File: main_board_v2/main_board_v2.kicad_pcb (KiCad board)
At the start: 2 copper layers, 13 parts, among them J1 Raspberry_Pi_4, U1 Pico, U2 Pico

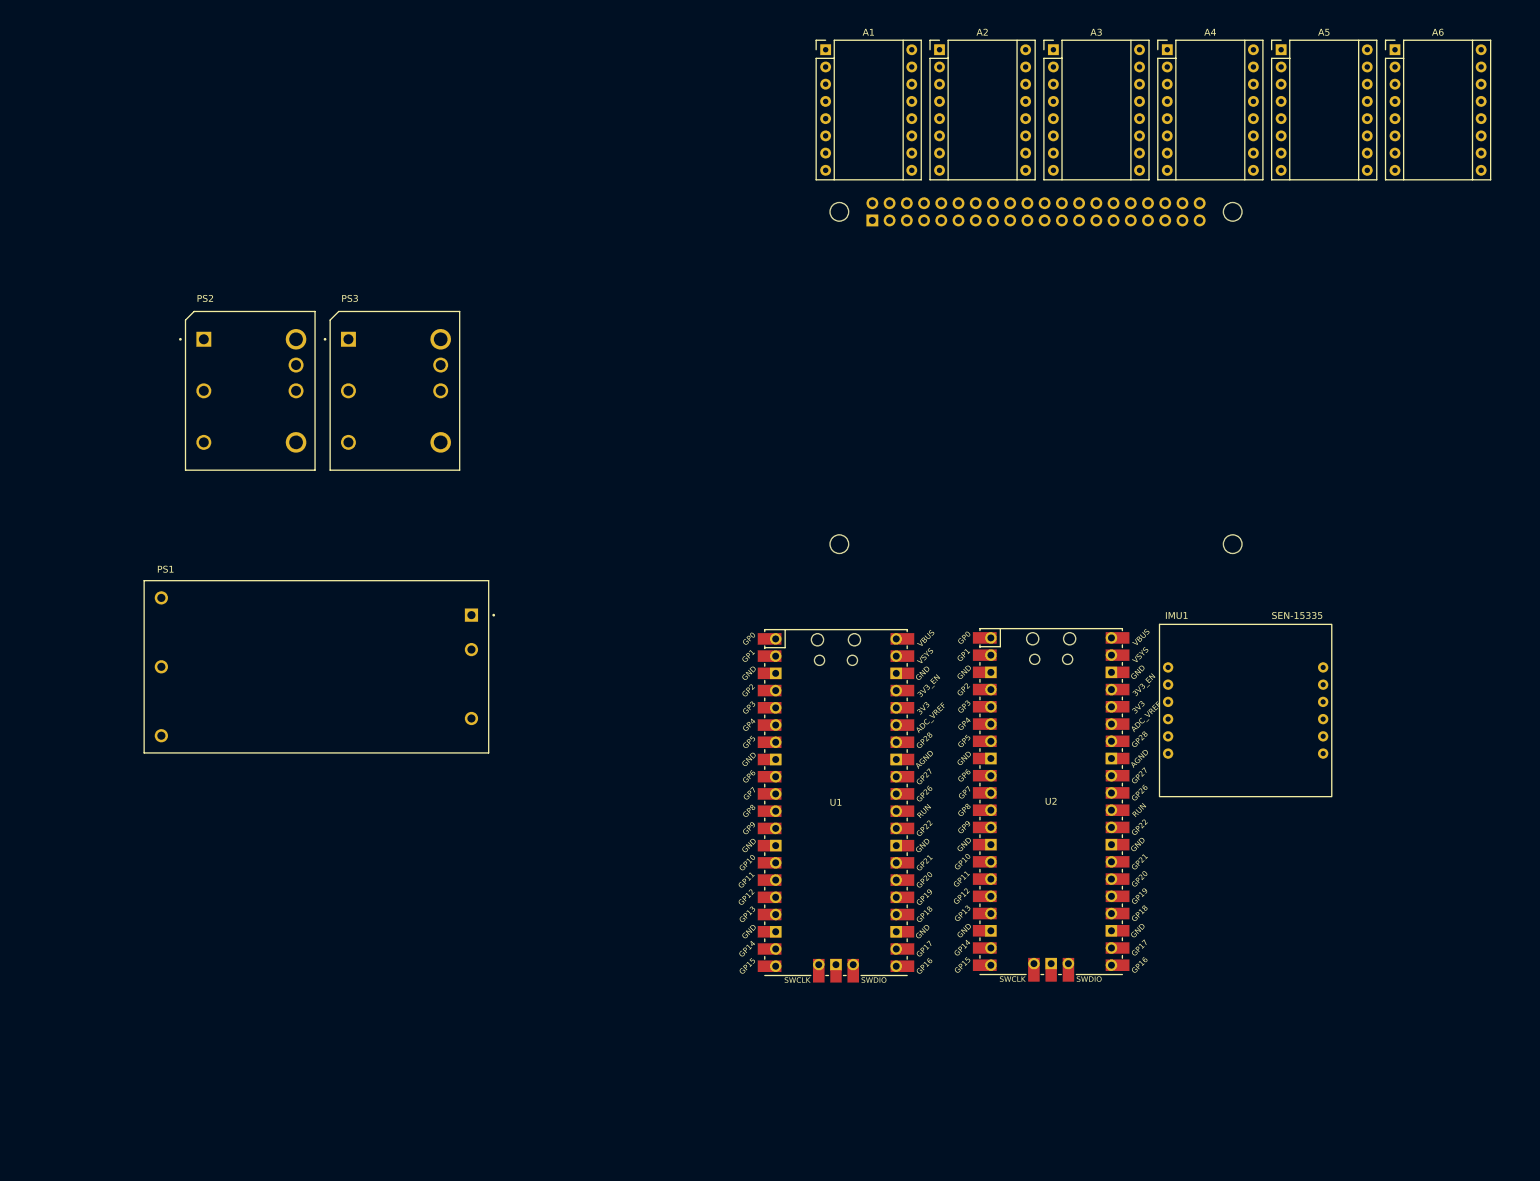
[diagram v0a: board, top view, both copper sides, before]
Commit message: Added headers and corrected 3d model of pico
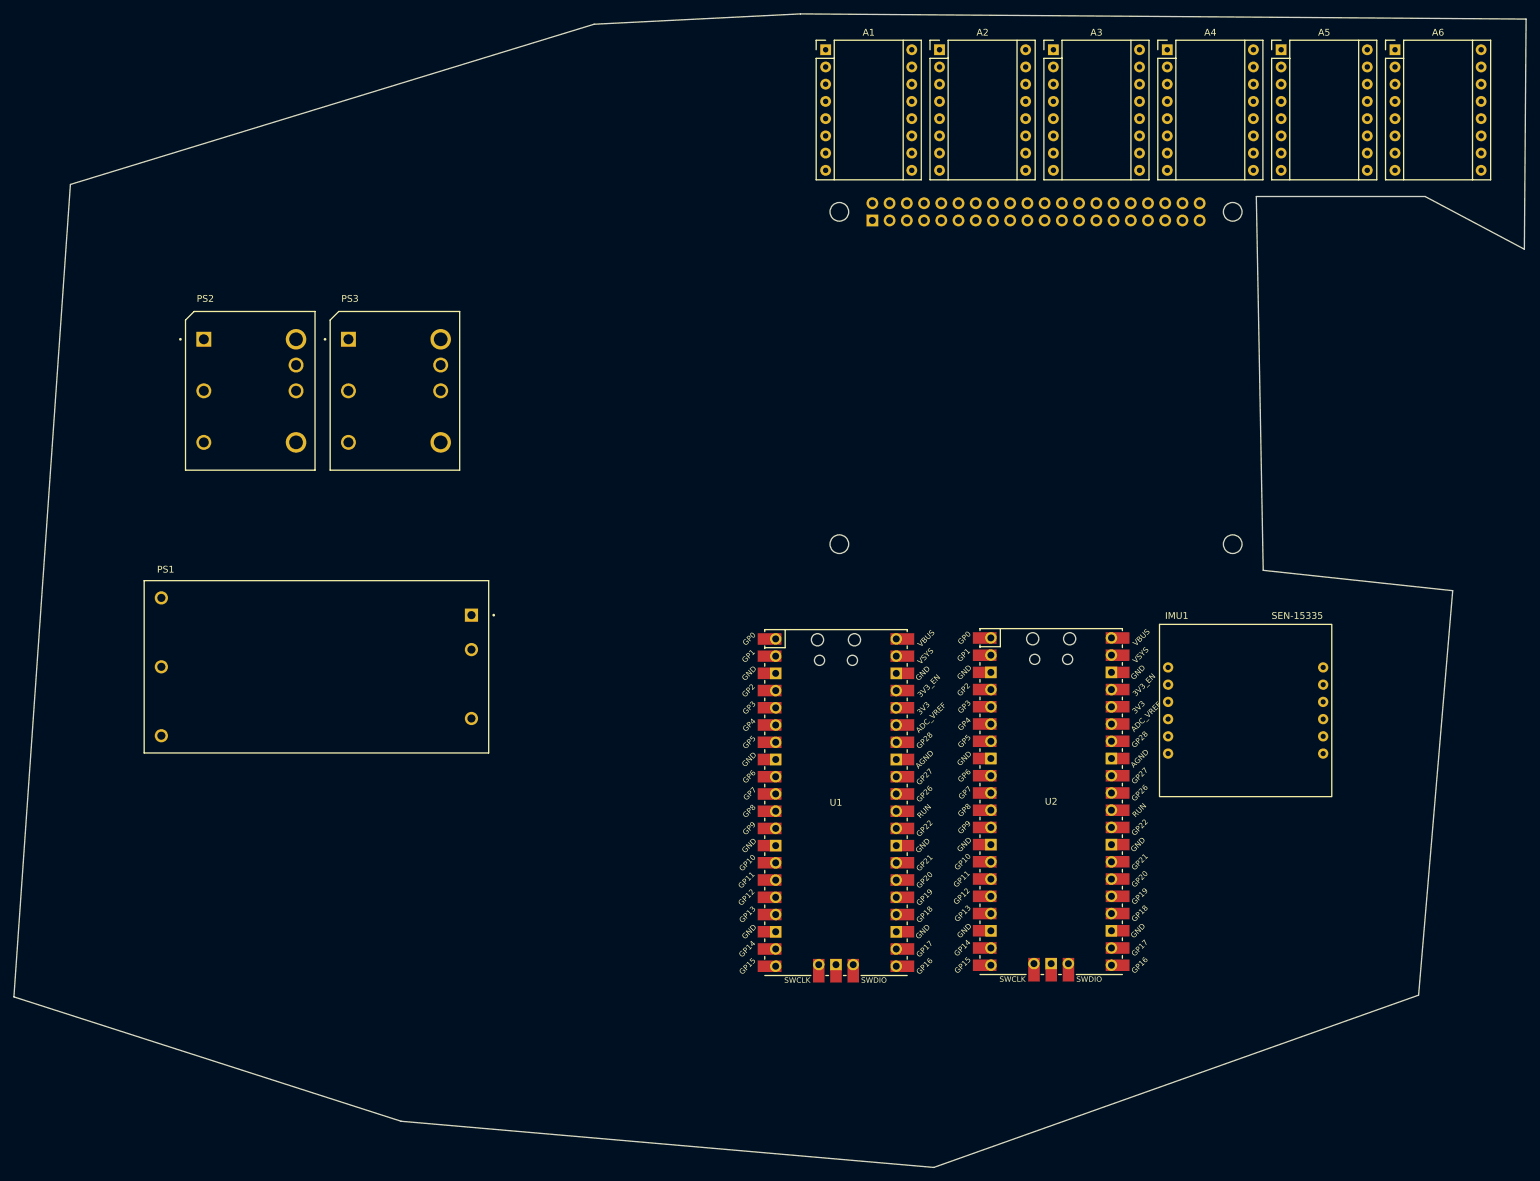
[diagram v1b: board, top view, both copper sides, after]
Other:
- board outline added: 223 x 170.1 mm

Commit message: Work, lots of
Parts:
- removed A5, A6: TMCSilentStepStick, Ensmasteel_librairy:TMCStick
- added BAU1: XT60-F, Connector_AMASS:AMASS_XT60-F_1x02_P7.20mm_Vertical, F.Cu at (124.4, 269.3)
- added Battery1: XT60-M, Connector_AMASS:AMASS_XT60-M_1x02_P7.20mm_Vertical, F.Cu at (149.2, 269.3)
- added C1: 100uF, Capacitor_THT:C_Radial_D6.3mm_H11.0mm_P2.50mm, F.Cu at (47.7, 136.2)
- added C10: 100uF, Capacitor_THT:C_Radial_D6.3mm_H11.0mm_P2.50mm, F.Cu at (32.0, 101.9)
- added C11: 100uF, Capacitor_THT:C_Radial_D6.3mm_H11.0mm_P2.50mm, F.Cu at (44.0, 81.7)
- added C12: 100uF, Capacitor_THT:C_Radial_D6.3mm_H11.0mm_P2.50mm, F.Cu at (44.0, 83.4)
- added C13: 1uF, Capacitor_SMD:C_0201_0603Metric, F.Cu at (32.0, 115.9)
- added C14: 1uF, Capacitor_SMD:C_0201_0603Metric, F.Cu at (44.0, 85.2)
- added C2: 1uF, Capacitor_SMD:C_0201_0603Metric, F.Cu at (47.7, 144.0)
- added C3: 100uF, Capacitor_THT:C_Radial_D6.3mm_H11.0mm_P2.50mm, F.Cu at (47.7, 151.9)
- added C4: 100uF, Capacitor_THT:C_Radial_D6.3mm_H11.0mm_P2.50mm, F.Cu at (47.7, 159.7)
- added C5: 100uF, Capacitor_THT:C_Radial_D6.3mm_H11.0mm_P2.50mm, F.Cu at (17.6, 87.8)
- added C6: 100uF, Capacitor_THT:C_Radial_D6.3mm_H11.0mm_P2.50mm, F.Cu at (17.6, 101.9)
- added C7: 100uF, Capacitor_THT:C_Radial_D6.3mm_H11.0mm_P2.50mm, F.Cu at (17.6, 115.9)
- added C8: 100uF, Capacitor_THT:C_Radial_D6.3mm_H11.0mm_P2.50mm, F.Cu at (17.6, 130.0)
- added C9: 100uF, Capacitor_THT:C_Radial_D6.3mm_H11.0mm_P2.50mm, F.Cu at (32.0, 87.8)
- added ERR1: LED, LED_SMD:LED_0805_2012Metric, F.Cu at (59.8, 50.9)
- added ERR2: LED, LED_SMD:LED_0805_2012Metric, F.Cu at (59.8, 54.0)
- added ERR3: LED, LED_SMD:LED_0805_2012Metric, F.Cu at (59.8, 57.0)
- added F1: Fuse, Fuse:Fuseholder_Blade_ATO_Littelfuse_Pudenz_2_Pin, F.Cu at (113.7, 259.4)
- added JP1: SolderJumper_2_Open, Jumper:SolderJumper-2_P1.3mm_Open_RoundedPad1.0x1.5mm, B.Cu at (117.6, 168.5)
- added JP2: SolderJumper_2_Open, Jumper:SolderJumper-2_P1.3mm_Open_RoundedPad1.0x1.5mm, B.Cu at (117.6, 164.9)
- added JP3: SolderJumper_2_Open, Jumper:SolderJumper-2_P1.3mm_Open_RoundedPad1.0x1.5mm, B.Cu at (117.6, 161.4)
- added LEDStrip1: JST PH 3, Connector_JST:JST_PH_B3B-PH-K_1x03_P2.00mm_Vertical, F.Cu at (37.9, 48.1)
- added PICO1_UART1: JST PH 3, Connector_JST:JST_PH_B3B-PH-K_1x03_P2.00mm_Vertical, F.Cu at (37.9, 54.6)
- added PICO1_swd1: JST PH 3, Connector_JST:JST_PH_B3B-PH-K_1x03_P2.00mm_Vertical, F.Cu at (31.2, 189.6)
- added PICO2_I2C1: JST PH 3, Connector_JST:JST_PH_B3B-PH-K_1x03_P2.00mm_Vertical, F.Cu at (37.7, 189.6)
- added PICO2_swd1: JST PH 3, Connector_JST:JST_PH_B3B-PH-K_1x03_P2.00mm_Vertical, F.Cu at (44.3, 189.6)
- added R1: 100R, Resistor_SMD:R_0201_0603Metric, F.Cu at (31.7, 173.0)
- added R2: 100R, Resistor_SMD:R_0201_0603Metric, F.Cu at (38.1, 173.0)
- added R3: 100R, Resistor_SMD:R_0201_0603Metric, F.Cu at (54.5, 142.3)
- added R4: 100R, Resistor_SMD:R_0201_0603Metric, F.Cu at (46.1, 69.7)
- added R5: 1k, Resistor_THT:R_Axial_DIN0207_L6.3mm_D2.5mm_P10.16mm_Horizontal, F.Cu at (82.9, 85.5)
- added R6: R_Trim, Potentiometer_THT:Potentiometer_Bourns_3296X_Horizontal, F.Cu at (54.5, 52.6)
- added R7: R_Trim, Potentiometer_THT:Potentiometer_Bourns_3296X_Horizontal, F.Cu at (54.5, 59.1)
- added RPI_PWMs1: JST PH 3, Connector_JST:JST_PH_B3B-PH-K_1x03_P2.00mm_Vertical, F.Cu at (37.9, 61.2)
- added RPI_SPI1: jst PH 01x4, Connector_JST:JST_PH_B4B-PH-K_1x04_P2.00mm_Vertical, F.Cu at (47.9, 65.0)
- added RPI_serial1: JST PH 3, Connector_JST:JST_PH_B3B-PH-K_1x03_P2.00mm_Vertical, F.Cu at (37.9, 67.7)
- added Servo1: 1x3_PinHeader, Connector_PinHeader_2.54mm:PinHeader_1x03_P2.54mm_Vertical, F.Cu at (183.6, 200.1)
- added Servo10: 1x3_PinHeader, Connector_PinHeader_2.54mm:PinHeader_1x03_P2.54mm_Vertical, F.Cu at (183.6, 241.9)
- added Servo11: 1x3_PinHeader, Connector_PinHeader_2.54mm:PinHeader_1x03_P2.54mm_Vertical, F.Cu at (183.6, 246.6)
- added Servo12: 1x3_PinHeader, Connector_PinHeader_2.54mm:PinHeader_1x03_P2.54mm_Vertical, F.Cu at (70.2, 70.8)
- added Servo2: 1x3_PinHeader, Connector_PinHeader_2.54mm:PinHeader_1x03_P2.54mm_Vertical, F.Cu at (183.6, 204.7)
- added Servo3: 1x3_PinHeader, Connector_PinHeader_2.54mm:PinHeader_1x03_P2.54mm_Vertical, F.Cu at (183.6, 209.4)
- added Servo4: 1x3_PinHeader, Connector_PinHeader_2.54mm:PinHeader_1x03_P2.54mm_Vertical, F.Cu at (183.6, 214.0)
- added Servo5: 1x3_PinHeader, Connector_PinHeader_2.54mm:PinHeader_1x03_P2.54mm_Vertical, F.Cu at (183.6, 218.7)
- added Servo6: 1x3_PinHeader, Connector_PinHeader_2.54mm:PinHeader_1x03_P2.54mm_Vertical, F.Cu at (183.6, 223.3)
- added Servo7: 1x3_PinHeader, Connector_PinHeader_2.54mm:PinHeader_1x03_P2.54mm_Vertical, F.Cu at (183.6, 228.0)
- added Servo8: 1x3_PinHeader, Connector_PinHeader_2.54mm:PinHeader_1x03_P2.54mm_Vertical, F.Cu at (183.6, 232.6)
- added Servo9: 1x3_PinHeader, Connector_PinHeader_2.54mm:PinHeader_1x03_P2.54mm_Vertical, F.Cu at (183.6, 237.3)
- added Stepper1: jst PH 01x4, Connector_JST:JST_PH_B4B-PH-K_1x04_P2.00mm_Vertical, F.Cu at (81.2, 247.7)
- added Stepper2: jst PH 01x4, Connector_JST:JST_PH_B4B-PH-K_1x04_P2.00mm_Vertical, F.Cu at (61.9, 253.5)
- added Stepper3: jst PH 01x4, Connector_JST:JST_PH_B4B-PH-K_1x04_P2.00mm_Vertical, F.Cu at (81.0, 214.9)
- added Stepper4: jst PH 01x4, Connector_JST:JST_PH_B4B-PH-K_1x04_P2.00mm_Vertical, F.Cu at (59.0, 210.6)
- added Tirette1: jst PH 01x4, Connector_JST:JST_PH_B4B-PH-K_1x04_P2.00mm_Vertical, F.Cu at (55.9, 147.1)
- added TiretteOK1: LED, LED_SMD:LED_0805_2012Metric, F.Cu at (59.8, 60.0)
- added U3: Pico, Ensmasteel_librairy:RPi_Pico_SMD_TH, F.Cu at (54.8, 138.2)
- PS1: value TEN_30-2423 -> I3A4W008A033V-001-R; footprint Ensmasteel_librairy:CONV_TEN_30-2423 -> Ensmasteel_librairy:CONV_I3A4W008A033V-001-R
- PS3: value I3A4W008A033V-001-R -> TEN_50-2423; footprint Ensmasteel_librairy:CONV_I3A4W008A033V-001-R -> Ensmasteel_librairy:CONV_TEN_30-2423
- U1: value Pico -> 4N25; footprint Ensmasteel_librairy:RPi_Pico_SMD_TH -> OptoDevice:Luna_NSL-32
- moved A1 233.2 mm to (90.5, 249.9), turned to 90 degrees
- moved A2 220.6 mm to (90.2, 233.3), turned to 90 degrees
- moved A3 209.6 mm to (90.2, 216.5), turned to 90 degrees
- moved A4 200.9 mm to (90.2, 199.7), turned to 90 degrees
- moved PS2 181.1 mm to (122.2, 234.0)
- moved PS3 169.8 mm to (147.7, 219.2), turned to -90 degrees
- moved J1 139.9 mm to (294.6, 83.7), turned to 90 degrees
- moved PS1 115.0 mm to (122.7, 203.5)
- moved IMU1 63.6 mm to (133.3, 143.3)
- moved U1 36.2 mm to (100.4, 150.2)
- moved U2 21.0 mm to (165.6, 151.6)
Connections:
- A1 pad 1: unconnected-(A1-GND-Pad1) -> GND
- A1 pad 10: unconnected-(A1-SDI/CFG1-Pad10) -> /CFG1
- A1 pad 11: unconnected-(A1-SCK/CFG2-Pad11) -> /CFG2
- A1 pad 12: unconnected-(A1-CS/CFG3-Pad12) -> /CFG3
- A1 pad 13: unconnected-(A1-SDO/UART/CFG0-Pad13) -> /CFG0
- A1 pad 15: unconnected-(A1-STEP-Pad15) -> /STEP1
- A1 pad 16: unconnected-(A1-DIR-Pad16) -> /DIR1
- A1 pad 2: unconnected-(A1-VIO-Pad2) -> /VIO_stepper_drivers
- A1 pad 3: unconnected-(A1-A2-Pad3) -> Net-(A1-A2)
- A1 pad 4: unconnected-(A1-A1-Pad4) -> Net-(A1-A1)
- A1 pad 5: unconnected-(A1-B1-Pad5) -> Net-(A1-B1)
- A1 pad 6: unconnected-(A1-B2-Pad6) -> Net-(A1-B2)
- A1 pad 7: unconnected-(A1-GND-Pad7) -> GND
- A1 pad 8: unconnected-(A1-VMOT-Pad8) -> /FusedProtectedVbatt
- A1 pad 9: unconnected-(A1-~{EN}-Pad9) -> /EN
- A2 pad 1: unconnected-(A2-GND-Pad1) -> GND
- A2 pad 10: unconnected-(A2-SDI/CFG1-Pad10) -> /CFG1
- A2 pad 11: unconnected-(A2-SCK/CFG2-Pad11) -> /CFG2
- A2 pad 12: unconnected-(A2-CS/CFG3-Pad12) -> /CFG3
- A2 pad 13: unconnected-(A2-SDO/UART/CFG0-Pad13) -> /CFG0
- A2 pad 15: unconnected-(A2-STEP-Pad15) -> /STEP3
- A2 pad 16: unconnected-(A2-DIR-Pad16) -> /DIR3
- A2 pad 2: unconnected-(A2-VIO-Pad2) -> /VIO_stepper_drivers
- A2 pad 3: unconnected-(A2-A2-Pad3) -> Net-(A2-A2)
- A2 pad 4: unconnected-(A2-A1-Pad4) -> Net-(A2-A1)
- A2 pad 5: unconnected-(A2-B1-Pad5) -> Net-(A2-B1)
- A2 pad 6: unconnected-(A2-B2-Pad6) -> Net-(A2-B2)
- A2 pad 7: unconnected-(A2-GND-Pad7) -> GND
- A2 pad 8: unconnected-(A2-VMOT-Pad8) -> /FusedProtectedVbatt
- A2 pad 9: unconnected-(A2-~{EN}-Pad9) -> /EN
- A3 pad 1: unconnected-(A3-GND-Pad1) -> GND
- A3 pad 10: unconnected-(A3-SDI/CFG1-Pad10) -> /CFG1
- A3 pad 11: unconnected-(A3-SCK/CFG2-Pad11) -> /CFG2
- A3 pad 12: unconnected-(A3-CS/CFG3-Pad12) -> /CFG3
- A3 pad 13: unconnected-(A3-SDO/UART/CFG0-Pad13) -> /CFG0
- A3 pad 15: unconnected-(A3-STEP-Pad15) -> /STEP4
- A3 pad 16: unconnected-(A3-DIR-Pad16) -> /DIR4
- A3 pad 2: unconnected-(A3-VIO-Pad2) -> /VIO_stepper_drivers
- A3 pad 3: unconnected-(A3-A2-Pad3) -> Net-(A3-A2)
- A3 pad 4: unconnected-(A3-A1-Pad4) -> Net-(A3-A1)
- A3 pad 5: unconnected-(A3-B1-Pad5) -> Net-(A3-B1)
- A3 pad 6: unconnected-(A3-B2-Pad6) -> Net-(A3-B2)
- A3 pad 7: unconnected-(A3-GND-Pad7) -> GND
- A3 pad 8: unconnected-(A3-VMOT-Pad8) -> /FusedProtectedVbatt
- A3 pad 9: unconnected-(A3-~{EN}-Pad9) -> /EN
- A4 pad 1: unconnected-(A4-GND-Pad1) -> GND
- A4 pad 10: unconnected-(A4-SDI/CFG1-Pad10) -> /CFG1
- A4 pad 11: unconnected-(A4-SCK/CFG2-Pad11) -> /CFG2
- A4 pad 12: unconnected-(A4-CS/CFG3-Pad12) -> /CFG3
- A4 pad 13: unconnected-(A4-SDO/UART/CFG0-Pad13) -> /CFG0
- A4 pad 15: unconnected-(A4-STEP-Pad15) -> /STEP2
- A4 pad 16: unconnected-(A4-DIR-Pad16) -> /DIR2
- A4 pad 2: unconnected-(A4-VIO-Pad2) -> /VIO_stepper_drivers
- A4 pad 3: unconnected-(A4-A2-Pad3) -> Net-(A4-A2)
- A4 pad 4: unconnected-(A4-A1-Pad4) -> Net-(A4-A1)
- A4 pad 5: unconnected-(A4-B1-Pad5) -> Net-(A4-B1)
- A4 pad 6: unconnected-(A4-B2-Pad6) -> Net-(A4-B2)
- A4 pad 7: unconnected-(A4-GND-Pad7) -> GND
- A4 pad 8: unconnected-(A4-VMOT-Pad8) -> /FusedProtectedVbatt
- A4 pad 9: unconnected-(A4-~{EN}-Pad9) -> /EN
- IMU1 pad 1: unconnected-(IMU1-VIN-Pad1) -> +3.3V
- IMU1 pad 11: unconnected-(IMU1-GND-Pad11) -> GND
- IMU1 pad 12: unconnected-(IMU1-GND-Pad12) -> GND
- IMU1 pad 2: unconnected-(IMU1-VIN-Pad2) -> +3.3V
- IMU1 pad 3: unconnected-(IMU1-DA-Pad3) -> /PI_SDA
- IMU1 pad 4: unconnected-(IMU1-CL-Pad4) -> /PI_SCL
- J1 pad 1: unconnected-(J1-3V3-Pad1) -> +3.3V
- J1 pad 10: unconnected-(J1-GPIO15/RXD-Pad10) -> Net-(J1-GPIO15/RXD)
- J1 pad 14: unconnected-(J1-GND-Pad14) -> GND
- J1 pad 15: unconnected-(J1-GPIO22-Pad15) -> /TIRETTE_input
- J1 pad 16: unconnected-(J1-GPIO23-Pad16) -> Net-(J1-GPIO23)
- J1 pad 17: unconnected-(J1-3V3-Pad17) -> +3.3V
- J1 pad 18: unconnected-(J1-GPIO24-Pad18) -> Net-(ERR1-A)
- J1 pad 2: unconnected-(J1-5V-Pad2) -> +5V
- J1 pad 20: unconnected-(J1-GND-Pad20) -> GND
- J1 pad 21: unconnected-(J1-MISO0/GPIO9-Pad21) -> /RPI_RX4
- J1 pad 22: unconnected-(J1-GPIO25-Pad22) -> Net-(ERR2-A)
- J1 pad 24: unconnected-(J1-~{CE0}/GPIO8-Pad24) -> /RPI_TX4
- J1 pad 25: unconnected-(J1-GND-Pad25) -> GND
- J1 pad 29: unconnected-(J1-GCLK1/GPIO5-Pad29) -> /RPI_RX3
- J1 pad 3: unconnected-(J1-SDA/GPIO2-Pad3) -> /PI_SDA
- J1 pad 30: unconnected-(J1-GND-Pad30) -> GND
- J1 pad 32: unconnected-(J1-PWM0/GPIO12-Pad32) -> Net-(J1-PWM0/GPIO12)
- J1 pad 33: unconnected-(J1-PWM1/GPIO13-Pad33) -> Net-(J1-PWM1/GPIO13)
- J1 pad 34: unconnected-(J1-GND-Pad34) -> GND
- J1 pad 35: unconnected-(J1-GPIO19/MISO1-Pad35) -> Net-(J1-GPIO19/MISO1)
- J1 pad 36: unconnected-(J1-GPIO16-Pad36) -> /LED_strip
- J1 pad 37: unconnected-(J1-GPIO26-Pad37) -> Net-(ERR3-A)
- J1 pad 38: unconnected-(J1-GPIO20/MOSI1-Pad38) -> Net-(J1-GPIO20/MOSI1)
- J1 pad 39: unconnected-(J1-GND-Pad39) -> GND
- J1 pad 4: unconnected-(J1-5V-Pad4) -> +5V
- J1 pad 40: unconnected-(J1-GPIO21/SCLK1-Pad40) -> Net-(J1-GPIO21/SCLK1)
- J1 pad 5: unconnected-(J1-SCL/GPIO3-Pad5) -> /PI_SCL
- J1 pad 6: unconnected-(J1-GND-Pad6) -> GND
- J1 pad 7: unconnected-(J1-GCLK0/GPIO4-Pad7) -> /RPI_TX3
- J1 pad 8: unconnected-(J1-GPIO14/TXD-Pad8) -> Net-(J1-GPIO14/TXD)
- J1 pad 9: unconnected-(J1-GND-Pad9) -> GND
- PS1 pad 1: unconnected-(PS1-+VIN(VCC)-Pad1) -> /ProtectedVbatt
- PS1 pad 2: unconnected-(PS1--VIN(GND)-Pad2) -> GND
- PS1 pad 3: unconnected-(PS1-REMOTE_ON/OFF-Pad3) -> GND
- PS1 pad 4: unconnected-(PS1-+VOUT-Pad4) -> GND
- PS1 pad 6: unconnected-(PS1--VOUT-Pad6) -> Net-(PS1-TRIM)
- PS2 pad 1: unconnected-(PS2-VIN(+)-Pad1) -> /ProtectedVbatt
- PS2 pad 2: unconnected-(PS2-~{ON}/OFF-Pad2) -> GND
- PS2 pad 3: unconnected-(PS2-VIN(-)/GND-Pad3) -> GND
- PS2 pad 4: unconnected-(PS2-VOUT(-)/GND-Pad4) -> GND
- PS2 pad 6: unconnected-(PS2-TRIM-Pad6) -> Net-(PS2-TRIM)
- PS2 pad 7: unconnected-(PS2-SENSE+-Pad7) -> +5VP
- PS2 pad 8: unconnected-(PS2-VOUT(+)-Pad8) -> +5VP
- PS3 pad 1: unconnected-(PS3-VIN(+)-Pad1) -> +BATT
- PS3 pad 2: unconnected-(PS3-~{ON}/OFF-Pad2) -> GND
- PS3 pad 4: unconnected-(PS3-VOUT(-)/GND-Pad4) -> +5V
- PS3 pad 6: unconnected-(PS3-TRIM-Pad6) -> GND
- U1 pad 1: unconnected-(U1-GPIO0-Pad1) -> Net-(Tirette1-Pin_3)
- U1 pad 2: unconnected-(U1-GPIO1-Pad2) -> GND
- U1 pad 4: unconnected-(U1-GPIO2-Pad4) -> /TIRETTE_input
- U2 pad 1: unconnected-(U2-GPIO0-Pad1) -> /RPI_pico1_TX0
- U2 pad 10: unconnected-(U2-GPIO7-Pad10) -> /STEP1
- U2 pad 11: unconnected-(U2-GPIO8-Pad11) -> /DIR1
- U2 pad 12: unconnected-(U2-GPIO9-Pad12) -> /STEP2
- U2 pad 13: unconnected-(U2-GND-Pad13) -> GND
- U2 pad 14: unconnected-(U2-GPIO10-Pad14) -> /DIR2
- U2 pad 15: unconnected-(U2-GPIO11-Pad15) -> /STEP3
- U2 pad 16: unconnected-(U2-GPIO12-Pad16) -> /DIR3
- U2 pad 17: unconnected-(U2-GPIO13-Pad17) -> /STEP4
- U2 pad 18: unconnected-(U2-GND-Pad18) -> GND
- U2 pad 19: unconnected-(U2-GPIO14-Pad19) -> /DIR4
- U2 pad 2: unconnected-(U2-GPIO1-Pad2) -> /RPI_pico1_RX0
- U2 pad 23: unconnected-(U2-GND-Pad23) -> GND
- U2 pad 25: unconnected-(U2-GPIO19-Pad25) -> Net-(JP3-B)
- U2 pad 26: unconnected-(U2-GPIO20-Pad26) -> Net-(JP2-B)
- U2 pad 27: unconnected-(U2-GPIO21-Pad27) -> Net-(JP1-B)
- U2 pad 28: unconnected-(U2-GND-Pad28) -> GND
- U2 pad 3: unconnected-(U2-GND-Pad3) -> GND
- U2 pad 38: unconnected-(U2-GND-Pad38) -> GND
- U2 pad 4: unconnected-(U2-GPIO2-Pad4) -> /EN
- U2 pad 40: unconnected-(U2-VBUS-Pad40) -> +5V
- U2 pad 41: unconnected-(U2-SWCLK-Pad41) -> Net-(PICO1_swd1-Pin_1)
- U2 pad 42: unconnected-(U2-GND-Pad42) -> GND
- U2 pad 43: unconnected-(U2-SWDIO-Pad43) -> Net-(PICO1_swd1-Pin_3)
- U2 pad 6: unconnected-(U2-GPIO4-Pad6) -> /RPI_RX3
- U2 pad 7: unconnected-(U2-GPIO5-Pad7) -> /RPI_TX3
- U2 pad 8: unconnected-(U2-GND-Pad8) -> GND
- U2 pad 9: unconnected-(U2-GPIO6-Pad9) -> /CFG3
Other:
- board size 223 x 170.1 mm -> 100 x 274 mm

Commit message: Work it seams
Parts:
- removed JP1, JP2, JP3: SolderJumper_2_Open, Jumper:SolderJumper-2_P1.3mm_Open_RoundedPad1.0x1.5mm
- added expansion1: Conn_01x17_Pin, Connector_PinHeader_2.54mm:PinHeader_1x17_P2.54mm_Vertical, F.Cu at (341.4, 119.0)
- C1, C10, C11, C12, C9, ERR1, ERR2, ERR3, TiretteOK1: moved to B.Cu
- C13, C14, C2: footprint Capacitor_SMD:C_0201_0603Metric -> Capacitor_SMD:C_0805_2012Metric
- R1, R2, R3, R4: footprint Resistor_SMD:R_0201_0603Metric -> Resistor_SMD:R_1206_3216Metric; moved to B.Cu
- R5: footprint Resistor_THT:R_Axial_DIN0207_L6.3mm_D2.5mm_P10.16mm_Horizontal -> Resistor_SMD:R_1206_3216Metric
- R6, R7: footprint Potentiometer_THT:Potentiometer_Bourns_3296X_Horizontal -> Potentiometer_THT:Potentiometer_Bourns_3296W_Vertical; moved to B.Cu
- U1: value 4N25 -> 4N35; footprint OptoDevice:Luna_NSL-32 -> Package_DIP:DIP-6_W7.62mm
- moved C5 344.9 mm to (313.5, 265.0), turned to 180 degrees
- moved C7 337.8 mm to (320.8, 264.9), turned to 135 degrees
- moved R6 330.4 mm to (305.1, 268.0)
- moved Servo12 328.7 mm to (340.4, 258.0), turned to -90 degrees
- moved C6 315.6 mm to (316.4, 203.5), turned to 180 degrees
- moved PICO2_swd1 314.3 mm to (327.9, 54.1), turned to 0 degrees
- moved R7 309.8 mm to (283.3, 268.0), turned to 180 degrees
- moved PICO2_I2C1 307.4 mm to (338.8, 127.8), turned to -90 degrees
- moved C13 300.8 mm to (331.7, 140.7), turned to 180 degrees
- moved C8 297.7 mm to (283.7, 263.4), turned to 135 degrees
- moved C9 296.3 mm to (276.0, 255.9), turned to 180 degrees
- moved C3 289.6 mm to (299.2, 295.4)
- moved C10 280.0 mm to (275.7, 239.9), turned to 180 degrees
- moved C11 271.4 mm to (275.8, 222.9), turned to 180 degrees
- moved U3 270.5 mm to (323.6, 168.2)
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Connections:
- A1 pad 2: /VIO_stepper_drivers -> /3V3PICO1
- A2 pad 2: /VIO_stepper_drivers -> /3V3PICO1
- A3 pad 2: /VIO_stepper_drivers -> /3V3PICO1
- A4 pad 2: /VIO_stepper_drivers -> /3V3PICO1
- RPI_SPI1 pad 1: GND -> Net-(J1-GPIO19/MISO1)
- RPI_SPI1 pad 2: Net-(J1-GPIO21/SCLK1) -> Net-(J1-GPIO20/MOSI1)
- RPI_SPI1 pad 3: Net-(J1-GPIO20/MOSI1) -> Net-(J1-GPIO21/SCLK1)
- RPI_SPI1 pad 4: Net-(J1-GPIO19/MISO1) -> GND
- U2 pad 10: /STEP1 -> unconnected-(U2-GPIO7-Pad10)
- U2 pad 12: /STEP2 -> /STEP1
- U2 pad 14: /DIR2 -> /DIR3
- U2 pad 16: /DIR3 -> /DIR4
- U2 pad 19: /DIR4 -> /DIR2
- U2 pad 20: unconnected-(U2-GPIO15-Pad20) -> /STEP2
- U2 pad 21: unconnected-(U2-GPIO16-Pad21) -> /CFG1
- U2 pad 22: unconnected-(U2-GPIO17-Pad22) -> /CFG2
- U2 pad 24: unconnected-(U2-GPIO18-Pad24) -> /CFG3
- U2 pad 25: Net-(JP3-B) -> /CFG0
- U2 pad 26: Net-(JP2-B) -> unconnected-(U2-GPIO20-Pad26)
- U2 pad 27: Net-(JP1-B) -> unconnected-(U2-GPIO21-Pad27)
- U2 pad 36: unconnected-(U2-3V3-Pad36) -> /3V3PICO1
- U2 pad 9: /CFG3 -> unconnected-(U2-GPIO6-Pad9)
- U3 pad 21: unconnected-(U3-GPIO16-Pad21) -> Net-(U3-GPIO16)
- U3 pad 22: unconnected-(U3-GPIO17-Pad22) -> Net-(U3-GPIO17)
- U3 pad 24: unconnected-(U3-GPIO18-Pad24) -> Net-(U3-GPIO18)
- U3 pad 25: unconnected-(U3-GPIO19-Pad25) -> Net-(U3-GPIO19)
- U3 pad 26: unconnected-(U3-GPIO20-Pad26) -> Net-(U3-GPIO20)
- U3 pad 27: unconnected-(U3-GPIO21-Pad27) -> Net-(U3-GPIO21)
- U3 pad 29: unconnected-(U3-GPIO22-Pad29) -> Net-(U3-GPIO22)
- U3 pad 30: unconnected-(U3-RUN-Pad30) -> Net-(U3-RUN)
- U3 pad 33: unconnected-(U3-AGND-Pad33) -> Net-(U3-AGND)
- U3 pad 34: unconnected-(U3-GPIO28_ADC2-Pad34) -> Net-(U3-GPIO28_ADC2)
- U3 pad 35: unconnected-(U3-ADC_VREF-Pad35) -> Net-(U3-ADC_VREF)
- U3 pad 36: unconnected-(U3-3V3-Pad36) -> Net-(U3-3V3)
- U3 pad 37: unconnected-(U3-3V3_EN-Pad37) -> Net-(U3-3V3_EN)
- U3 pad 39: unconnected-(U3-VSYS-Pad39) -> Net-(U3-VSYS)
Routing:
- net +BATT: track 0.00 -> 378.8 mm, vias 0 -> 2
- net +5VP: track 0.00 -> 313.9 mm, vias 0 -> 1
- net +5V: track 0.00 -> 182.5 mm
- net Net-(PICO1_swd1-Pin_3): track 0.00 -> 163.4 mm, vias 0 -> 2
- net Net-(PICO1_swd1-Pin_1): track 0.00 -> 158.8 mm, vias 0 -> 2
- net +3.3V: track 0.00 -> 145.5 mm, vias 0 -> 2
- net Net-(PICO2_swd1-Pin_1): track 0.00 -> 140.9 mm, vias 0 -> 1
- net Net-(PICO2_swd1-Pin_3): track 0.00 -> 140.4 mm, vias 0 -> 1
- net /FusedProtectedVbatt: track 0.00 -> 136.7 mm
- net /EN: track 0.00 -> 118.2 mm
- net /3V3PICO1: track 0.00 -> 117.1 mm
- net /RPI_TX4: track 0.00 -> 92.2 mm, vias 0 -> 1
- net /servo11: track 0.00 -> 88.9 mm, vias 0 -> 1
- net /DIR1: track 0.00 -> 87.1 mm
- net /RPI_RX4: track 0.00 -> 85.6 mm
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- added copper zone on B.Cu, net GND
- added copper zone on F.Cu, net GND
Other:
- board text added: "Vincent Belpois 2023"
- board text added: "ezBot"
